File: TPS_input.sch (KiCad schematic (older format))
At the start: 3 parts, among them P48 CONN_1, P49 CONN_1, P50 CONN_1

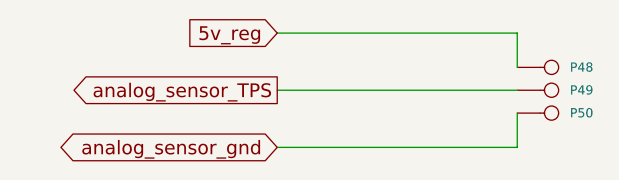
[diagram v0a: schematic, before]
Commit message: DFH mans up a bit. Perhaps usable for something at this point, like making trips to the local store ;)
I connected TA pins to sub circuits, fixed a number if items discussed in the DIYEFI forums. This is it's 21st version, so it was time for it to man up a bit, and become something potentially useful.

Signed-off-by: Jared Harvey <TortiseGIT@jaredharvey.com>
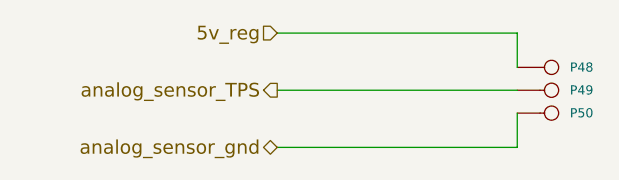
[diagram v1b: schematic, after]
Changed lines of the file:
@@
-EESchema Schematic File Version 1
-LIBS:power,./freeEMS_lib,device,conn,linear,regul,74xx,cmos4000,adc-dac,memory,xilinx,special,microcontrollers,dsp,microchip,analog_switches,motorola,texas,intel,audio,interface,digital-audio,philips,display,cypress,siliconi,contrib,valves,./freeEMS_1.cache
-EELAYER 23  0
+EESchema Schematic File Version 2  date 9/10/2011 11:43:52 AM
+LIBS:power
+LIBS:freeEMS_lib
+LIBS:device
+LIBS:conn
+LIBS:linear
+LIBS:regul
+LIBS:74xx
+LIBS:cmos4000
+LIBS:adc-dac
+LIBS:memory
+LIBS:xilinx
+LIBS:special
+LIBS:microcontrollers
+LIBS:dsp
+LIBS:microchip
+LIBS:analog_switches
+LIBS:motorola
+LIBS:texas
+LIBS:intel
+LIBS:audio
+LIBS:interface
+LIBS:digital-audio
+LIBS:philips
+LIBS:display
+LIBS:cypress
+LIBS:siliconi
+LIBS:contrib
+LIBS:valves
+LIBS:freeEMS_1-cache
+EELAYER 25  0
 EELAYER END
 $Descr A4 11700 8267
+encoding utf-8
 Sheet 38 41
-Title "freeEMS 1.0"
-Date "15 nov 2008"
-Rev "A.20"
-Comp "diyefi.org"
+Title "DFH for freeEMS"
+Date "10 sep 2011"
+Rev "A.21"
+Comp "FreeEMS.org"
 Comment1 "TPS_input.sch"
 Comment2 ""
@@
 U 1 1 48AA1ACF
 P 4450 2050
-F 0 "P50" H 4530 2050 40  0000 L C
-F 1 "CONN_1" H 4450 2105 30  0001 C C
-F 2 "1PIN" V 1130 2600 60  0001 C C
+F 0 "P50" H 4530 2050 40  0000 L CNN
+F 1 "CONN_1" H 4450 2105 30  0001 C CNN
+F 2 "1PIN" V 1130 2600 60  0001 C CNN
 	1    4450 2050
 	1    0    0    -1
@@
 U 1 1 48AA1ACC
 P 4450 1950
-F 0 "P49" H 4530 1950 40  0000 L C
-F 1 "CONN_1" H 4450 2005 30  0001 C C
-F 2 "1PIN" V 1130 2600 60  0001 C C
+F 0 "P49" H 4530 1950 40  0000 L CNN
+F 1 "CONN_1" H 4450 2005 30  0001 C CNN
+F 2 "1PIN" V 1130 2600 60  0001 C CNN
 	1    4450 1950
 	1    0    0    -1
@@
 U 1 1 48AA1AC9
 P 4450 1850
-F 0 "P48" H 4530 1850 40  0000 L C
-F 1 "CONN_1" H 4450 1905 30  0001 C C
-F 2 "1PIN" V 1130 2600 60  0001 C C
+F 0 "P48" H 4530 1850 40  0000 L CNN
+F 1 "CONN_1" H 4450 1905 30  0001 C CNN
+F 2 "1PIN" V 1130 2600 60  0001 C CNN
 	1    4450 1850
 	1    0    0    -1
@@
 Wire Wire Line
 	4300 1700 4300 1850
-Text GLabel 3250 1700 0    60   Input
+Text HLabel 3250 1700 0    60   Input ~ 0
 5v_reg
-Text GLabel 3250 2200 0    60   BiDi
+Text HLabel 3250 2200 0    60   BiDi ~ 0
 analog_sensor_gnd
-Text GLabel 3250 1950 0    60   Output
+Text HLabel 3250 1950 0    60   Output ~ 0
 analog_sensor_TPS
 $EndSCHEMATC
